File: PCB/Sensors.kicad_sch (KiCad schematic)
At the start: 9 parts, among them U401 MMC5633NJL, U402 LSM6DSV320, U403 MS5607-02BA, U404 SAM-M8Q

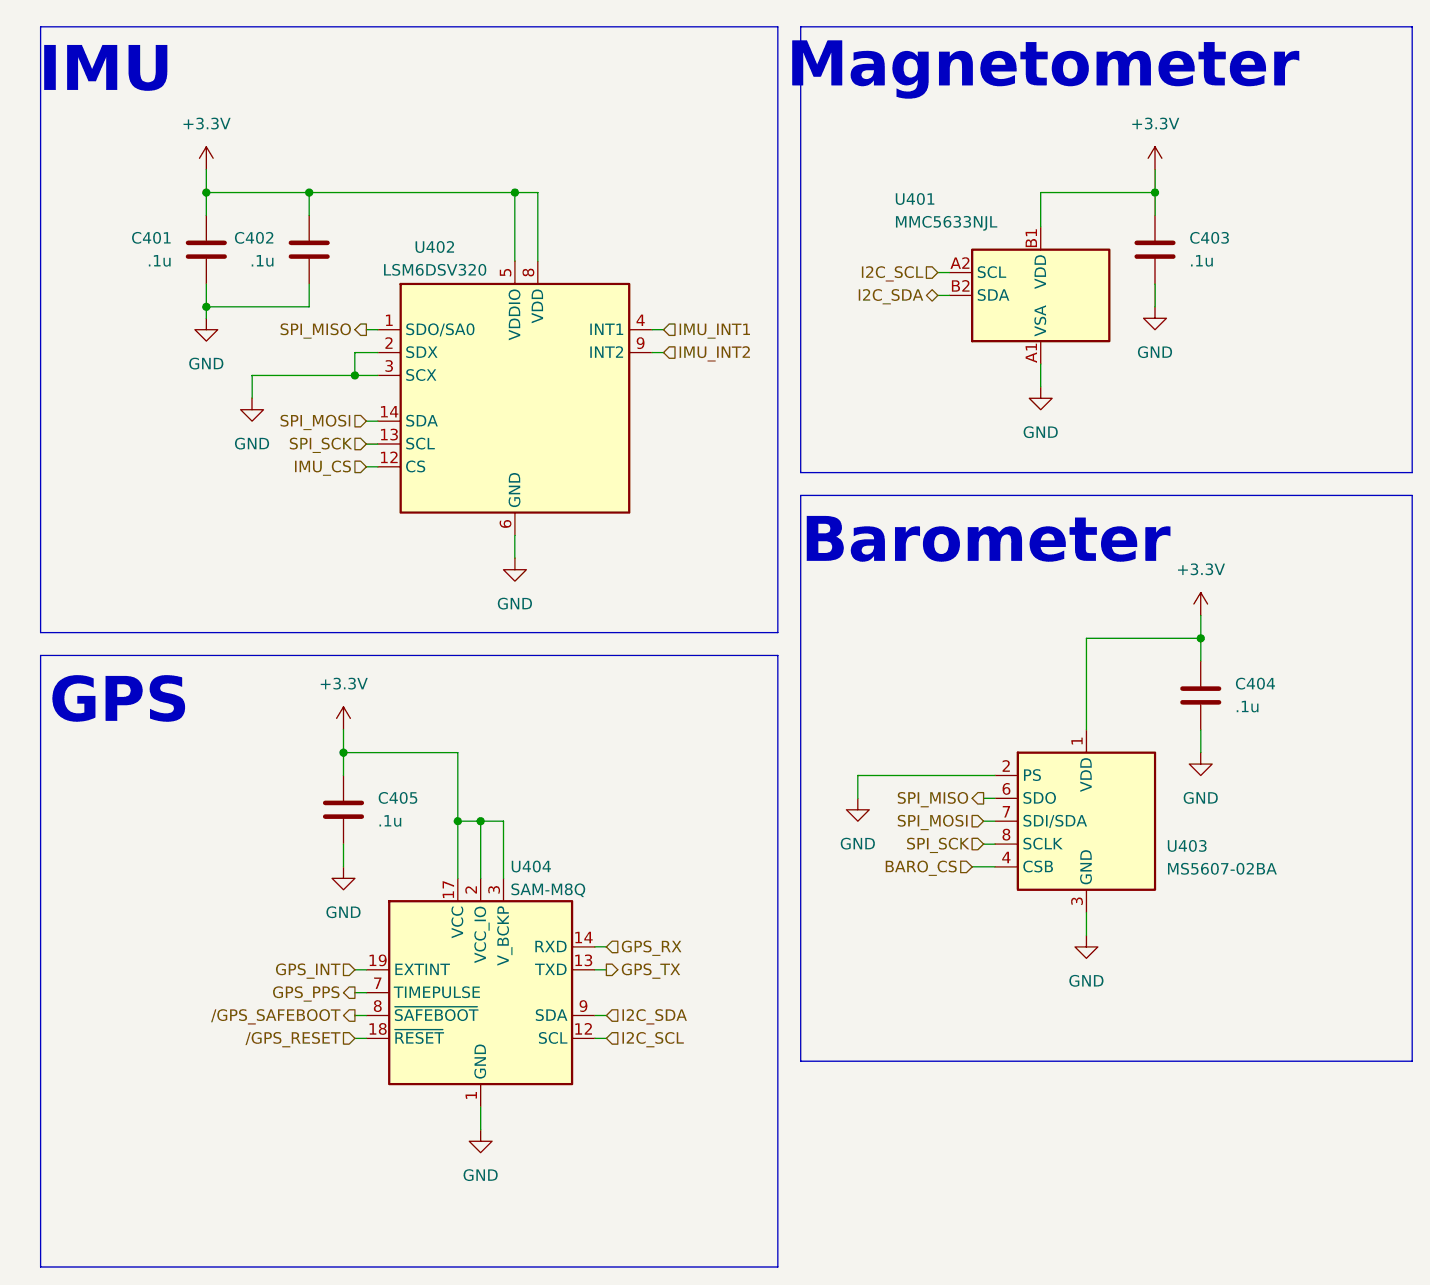
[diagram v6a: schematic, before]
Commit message: - Swapped out 2 LED's for neopixels- Added reverse polarity protection- Replaced Radio module with deticated IC and passives
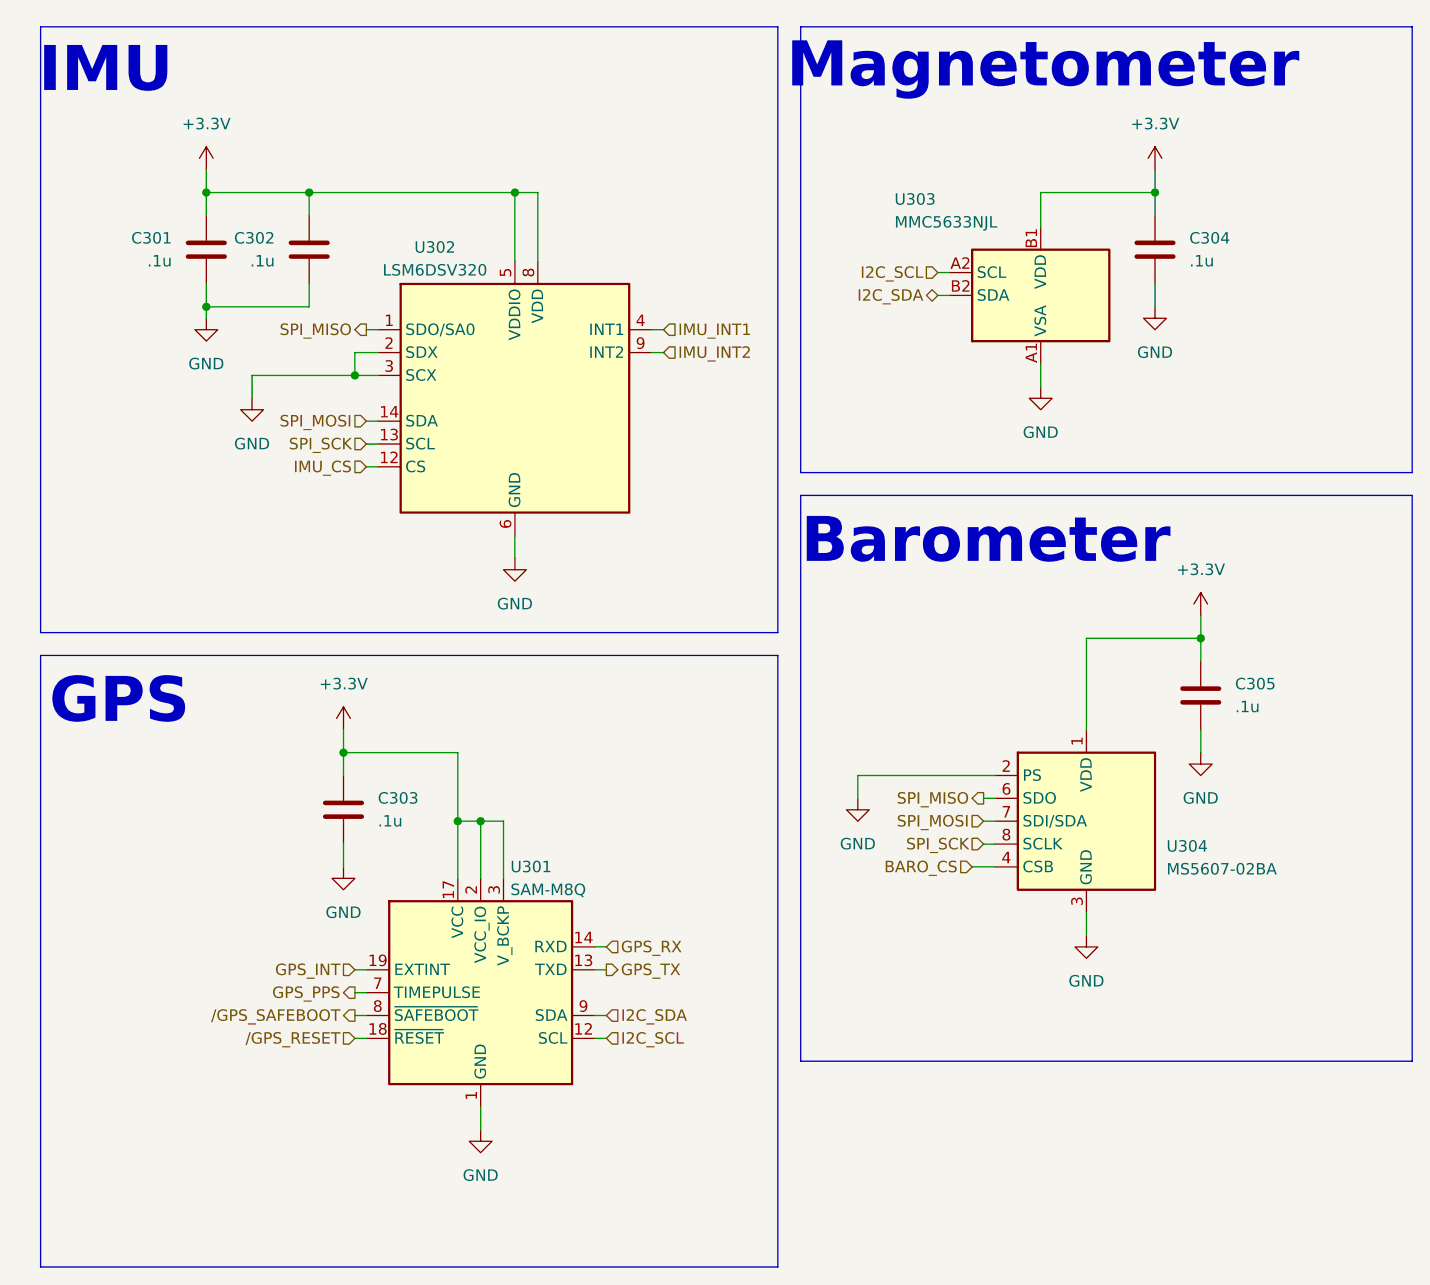
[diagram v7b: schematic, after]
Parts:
- renumbered C401 to C301, C402 to C302, C405 to C303, C403 to C304, C404 to C305, U404 to U301, U402 to U302, U401 to U303, U403 to U304
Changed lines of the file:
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@@
 		(dnp no)
 		(fields_autoplaced yes)
-		(property "Reference" "#PWR0403"
+		(property "Reference" "#PWR0312"
 			(at 140.97 54.61 0)
 			(hide yes)
@@
 			(project "Flight Computer"
 				(path "/4254ccd1-49f4-4fe6-9bf7-ccb200d73af4/c6ca0e5c-eb30-4ed2-9f63-dd4973f3175a"
-					(reference "#PWR0403")
+					(reference "#PWR0312")
 					(unit 1)
 				)
@@
 		(dnp no)
 		(fields_autoplaced yes)
-		(property "Reference" "#PWR0412"
+		(property "Reference" "#PWR0305"
 			(at 50.8 116.84 0)
 			(hide yes)
@@
 			(project "Flight Computer"
 				(path "/4254ccd1-49f4-4fe6-9bf7-ccb200d73af4/c6ca0e5c-eb30-4ed2-9f63-dd4973f3175a"
-					(reference "#PWR0412")
+					(reference "#PWR0305")
 					(unit 1)
 				)
@@
 		(in_pos_files yes)
 		(dnp no)
-		(property "Reference" "U404"
+		(property "Reference" "U301"
 			(at 69.342 110.49 0)
 			(show_name no)
@@
 			(project "Flight Computer"
 				(path "/4254ccd1-49f4-4fe6-9bf7-ccb200d73af4/c6ca0e5c-eb30-4ed2-9f63-dd4973f3175a"
-					(reference "U404")
+					(reference "U301")
 					(unit 1)
 				)
@@
 		(in_pos_files yes)
 		(dnp no)
-		(property "Reference" "C404"
+		(property "Reference" "C305"
 			(at 149.86 90.1699 0)
 			(show_name no)
@@
 			(project "Flight Computer"
 				(path "/4254ccd1-49f4-4fe6-9bf7-ccb200d73af4/c6ca0e5c-eb30-4ed2-9f63-dd4973f3175a"
-					(reference "C404")
+					(reference "C305")
 					(unit 1)
 				)
@@
 		(dnp no)
 		(fields_autoplaced yes)
-		(property "Reference" "#PWR0414"
+		(property "Reference" "#PWR0310"
 			(at 133.35 124.46 0)
 			(hide yes)
@@
 			(project "Flight Computer"
 				(path "/4254ccd1-49f4-4fe6-9bf7-ccb200d73af4/c6ca0e5c-eb30-4ed2-9f63-dd4973f3175a"
-					(reference "#PWR0414")
+					(reference "#PWR0310")
 					(unit 1)
 				)
@@
 		(dnp no)
 		(fields_autoplaced yes)
-		(property "Reference" "#PWR0408"
+		(property "Reference" "#PWR0313"
 			(at 146.05 86.36 0)
 			(hide yes)
@@
 			(project "Flight Computer"
 				(path "/4254ccd1-49f4-4fe6-9bf7-ccb200d73af4/c6ca0e5c-eb30-4ed2-9f63-dd4973f3175a"
-					(reference "#PWR0408")
+					(reference "#PWR0313")
 					(unit 1)
 				)
@@
 		(dnp no)
 		(fields_autoplaced yes)
-		(property "Reference" "#PWR0405"
+		(property "Reference" "#PWR0309"
 			(at 128.27 63.5 0)
 			(hide yes)
@@
 			(project "Flight Computer"
 				(path "/4254ccd1-49f4-4fe6-9bf7-ccb200d73af4/c6ca0e5c-eb30-4ed2-9f63-dd4973f3175a"
-					(reference "#PWR0405")
+					(reference "#PWR0309")
 					(unit 1)
 				)
@@
 		(in_pos_files yes)
 		(dnp no)
-		(property "Reference" "U401"
+		(property "Reference" "U303"
 			(at 112.014 36.322 0)
 			(show_name no)
@@
 			(project "Flight Computer"
 				(path "/4254ccd1-49f4-4fe6-9bf7-ccb200d73af4/c6ca0e5c-eb30-4ed2-9f63-dd4973f3175a"
-					(reference "U401")
+					(reference "U303")
 					(unit 1)
 				)
@@
 		(in_pos_files yes)
 		(dnp no)
-		(property "Reference" "C403"
+		(property "Reference" "C304"
 			(at 144.78 40.6399 0)
 			(show_name no)
@@
 			(project "Flight Computer"
 				(path "/4254ccd1-49f4-4fe6-9bf7-ccb200d73af4/c6ca0e5c-eb30-4ed2-9f63-dd4973f3175a"
-					(reference "C403")
+					(reference "C304")
 					(unit 1)
 				)
@@
 		(in_pos_files yes)
 		(dnp no)
-		(property "Reference" "U402"
+		(property "Reference" "U302"
 			(at 60.96 41.656 0)
 			(show_name no)
@@
 			(project "Flight Computer"
 				(path "/4254ccd1-49f4-4fe6-9bf7-ccb200d73af4/c6ca0e5c-eb30-4ed2-9f63-dd4973f3175a"
-					(reference "U402")
+					(reference "U302")
 					(unit 1)
 				)
@@
 		(dnp no)
 		(fields_autoplaced yes)
-		(property "Reference" "#PWR0416"
+		(property "Reference" "#PWR0306"
 			(at 66.04 146.05 0)
 			(hide yes)
@@
 			(project "Flight Computer"
 				(path "/4254ccd1-49f4-4fe6-9bf7-ccb200d73af4/c6ca0e5c-eb30-4ed2-9f63-dd4973f3175a"
-					(reference "#PWR0416")
+					(reference "#PWR0306")
 					(unit 1)
 				)
@@
 		(dnp no)
 		(fields_autoplaced yes)
-		(property "Reference" "#PWR0409"
+		(property "Reference" "#PWR0304"
 			(at 50.8 99.06 0)
 			(hide yes)
@@
 			(project "Flight Computer"
 				(path "/4254ccd1-49f4-4fe6-9bf7-ccb200d73af4/c6ca0e5c-eb30-4ed2-9f63-dd4973f3175a"
-					(reference "#PWR0409")
+					(reference "#PWR0304")
 					(unit 1)
 				)
@@
 		(dnp no)
 		(fields_autoplaced yes)
-		(property "Reference" "#PWR0407"
+		(property "Reference" "#PWR0307"
 			(at 69.85 82.55 0)
 			(hide yes)
@@
 			(project "Flight Computer"
 				(path "/4254ccd1-49f4-4fe6-9bf7-ccb200d73af4/c6ca0e5c-eb30-4ed2-9f63-dd4973f3175a"
-					(reference "#PWR0407")
+					(reference "#PWR0307")
 					(unit 1)
 				)
@@
 		(dnp no)
 		(fields_autoplaced yes)
-		(property "Reference" "#PWR0411"
+		(property "Reference" "#PWR0308"
 			(at 107.95 109.22 0)
 			(hide yes)
@@
 			(project "Flight Computer"
 				(path "/4254ccd1-49f4-4fe6-9bf7-ccb200d73af4/c6ca0e5c-eb30-4ed2-9f63-dd4973f3175a"
-					(reference "#PWR0411")
+					(reference "#PWR0308")
 					(unit 1)
 				)
@@
 		(in_pos_files yes)
 		(dnp no)
-		(property "Reference" "C405"
+		(property "Reference" "C303"
 			(at 54.61 102.8699 0)
 			(show_name no)
@@
 			(project "Flight Computer"
 				(path "/4254ccd1-49f4-4fe6-9bf7-ccb200d73af4/c6ca0e5c-eb30-4ed2-9f63-dd4973f3175a"
-					(reference "C405")
+					(reference "C303")
 					(unit 1)
 				)
@@
 		(in_pos_files yes)
 		(dnp no)
-		(property "Reference" "U403"
+		(property "Reference" "U304"
 			(at 142.24 108.204 0)
 			(show_name no)
@@
 			(project "Flight Computer"
 				(path "/4254ccd1-49f4-4fe6-9bf7-ccb200d73af4/c6ca0e5c-eb30-4ed2-9f63-dd4973f3175a"
-					(reference "U403")
+					(reference "U304")
 					(unit 1)
 				)
@@
 		(in_pos_files yes)
 		(dnp no)
-		(property "Reference" "C402"
+		(property "Reference" "C302"
 			(at 43.18 40.6399 0)
 			(show_name no)
@@
 			(project "Flight Computer"
 				(path "/4254ccd1-49f4-4fe6-9bf7-ccb200d73af4/c6ca0e5c-eb30-4ed2-9f63-dd4973f3175a"
-					(reference "C402")
+					(reference "C302")
 					(unit 1)
 				)
@@
 		(in_pos_files yes)
 		(dnp no)
-		(property "Reference" "C401"
+		(property "Reference" "C301"
 			(at 31.75 40.6399 0)
 			(show_name no)
@@
 			(project "Flight Computer"
 				(path "/4254ccd1-49f4-4fe6-9bf7-ccb200d73af4/c6ca0e5c-eb30-4ed2-9f63-dd4973f3175a"
-					(reference "C401")
+					(reference "C301")
 					(unit 1)
 				)
@@
 		(dnp no)
 		(fields_autoplaced yes)
-		(property "Reference" "#PWR0410"
+		(property "Reference" "#PWR0314"
 			(at 146.05 104.14 0)
 			(hide yes)
@@
 			(project "Flight Computer"
 				(path "/4254ccd1-49f4-4fe6-9bf7-ccb200d73af4/c6ca0e5c-eb30-4ed2-9f63-dd4973f3175a"
-					(reference "#PWR0410")
+					(reference "#PWR0314")
 					(unit 1)
 				)
@@
 		(dnp no)
 		(fields_autoplaced yes)
-		(property "Reference" "#PWR0402"
+		(property "Reference" "#PWR0311"
 			(at 140.97 36.83 0)
 			(hide yes)
@@
 			(project "Flight Computer"
 				(path "/4254ccd1-49f4-4fe6-9bf7-ccb200d73af4/c6ca0e5c-eb30-4ed2-9f63-dd4973f3175a"
-					(reference "#PWR0402")
+					(reference "#PWR0311")
 					(unit 1)
 				)
@@
 		(dnp no)
 		(fields_autoplaced yes)
-		(property "Reference" "#PWR0406"
+		(property "Reference" "#PWR0303"
 			(at 40.64 64.77 0)
 			(hide yes)
@@
 			(project "Flight Computer"
 				(path "/4254ccd1-49f4-4fe6-9bf7-ccb200d73af4/c6ca0e5c-eb30-4ed2-9f63-dd4973f3175a"
-					(reference "#PWR0406")
+					(reference "#PWR0303")
 					(unit 1)
 				)
@@
 		(dnp no)
 		(fields_autoplaced yes)
-		(property "Reference" "#PWR0401"
+		(property "Reference" "#PWR0301"
 			(at 35.56 36.83 0)
 			(hide yes)
@@
 			(project "Flight Computer"
 				(path "/4254ccd1-49f4-4fe6-9bf7-ccb200d73af4/c6ca0e5c-eb30-4ed2-9f63-dd4973f3175a"
-					(reference "#PWR0401")
+					(reference "#PWR0301")
 					(unit 1)
 				)
@@
 		(dnp no)
 		(fields_autoplaced yes)
-		(property "Reference" "#PWR0404"
+		(property "Reference" "#PWR0302"
 			(at 35.56 55.88 0)
 			(hide yes)
@@
 			(project "Flight Computer"
 				(path "/4254ccd1-49f4-4fe6-9bf7-ccb200d73af4/c6ca0e5c-eb30-4ed2-9f63-dd4973f3175a"
-					(reference "#PWR0404")
-					(unit 1)
-				)
+					(reference "#PWR0302")
+					(unit 1)
+				)

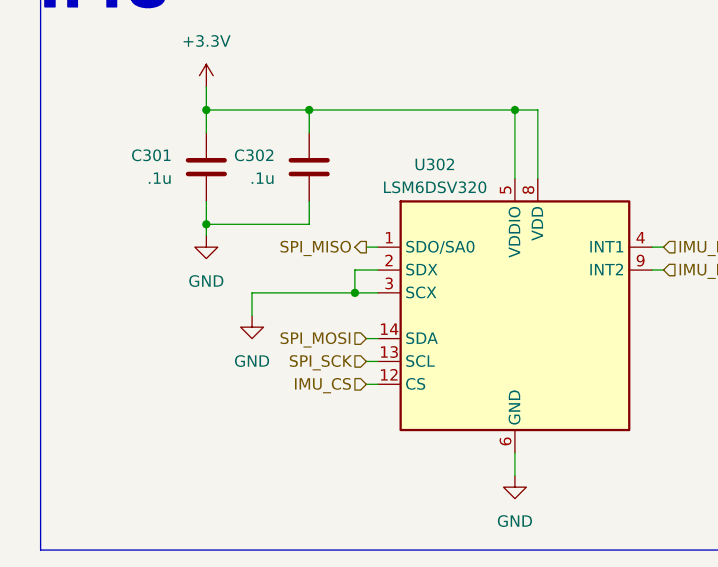
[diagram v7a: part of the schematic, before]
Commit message: - Renamed all NETs connected to MCU sheet to the pin name - Cleaned up schematic - Named all unnamed NETs
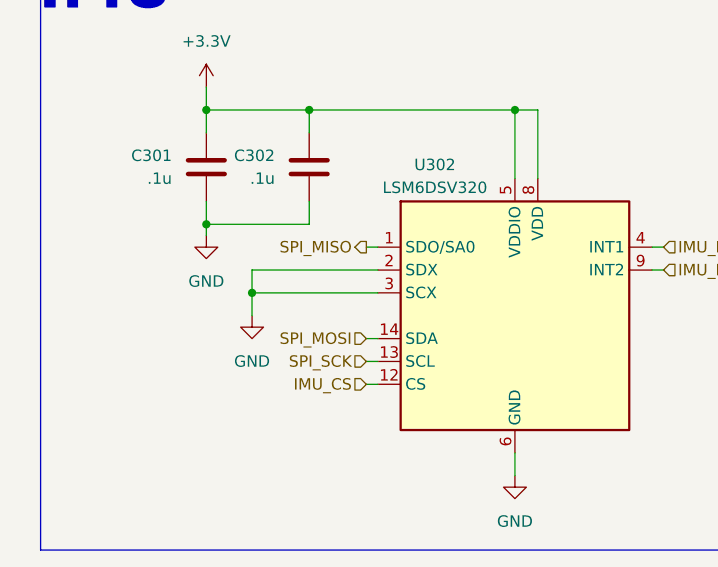
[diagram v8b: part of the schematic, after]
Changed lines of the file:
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@@
+	)
+	(junction
+		(at 40.64 55.88)
+		(diameter 0)
+		(color 0 0 0 0)
 	)
 	(junction
@@
 	)
 	(junction
-		(at 52.07 55.88)
-		(diameter 0)
-		(color 0 0 0 0)
-	)
-	(junction
 		(at 140.97 35.56)
 		(diameter 0)
@@
 	(wire
 		(pts
-			(xy 52.07 55.88) (xy 52.07 53.34)
+			(xy 40.64 55.88) (xy 40.64 53.34)
 		)
 		(stroke
@@
 	(wire
 		(pts
-			(xy 40.64 55.88) (xy 52.07 55.88)
+			(xy 40.64 55.88) (xy 54.61 55.88)
 		)
 		(stroke
@@
 	(wire
 		(pts
-			(xy 52.07 53.34) (xy 54.61 53.34)
+			(xy 40.64 53.34) (xy 54.61 53.34)
 		)
 		(stroke
@@
 		)
 		(stroke
-			(width 0)
-			(type default)
-		)
-	)
-	(wire
-		(pts
-			(xy 54.61 55.88) (xy 52.07 55.88)
-		)
-		(stroke
